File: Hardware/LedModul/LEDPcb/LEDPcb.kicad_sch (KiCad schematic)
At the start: 27 parts, among them J1 Conn_01x01_Pin, J2 Conn_01x01_Pin

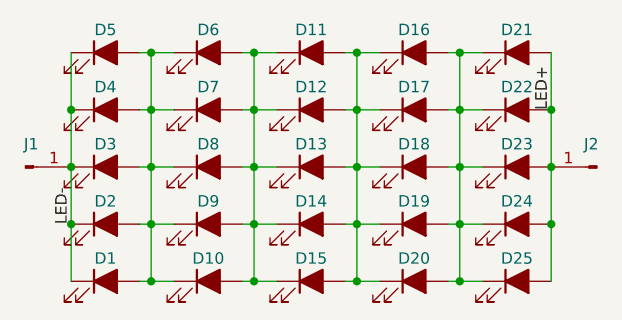
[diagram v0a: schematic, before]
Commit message: added panel
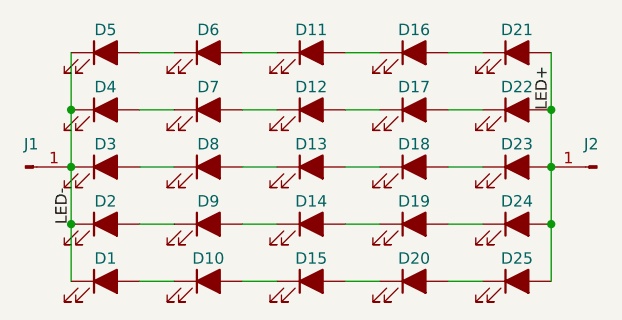
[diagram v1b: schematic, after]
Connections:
- new net: D5.2 (A), D6.1 (K)
- new net: D11.1 (K), D6.2 (A)
- new net: D3.2 (A), D8.1 (K)
- new net: D13.1 (K), D8.2 (A)
- new net: D19.2 (A), D24.1 (K)
- new net: D11.2 (A), D16.1 (K)
- new net: D16.2 (A), D21.1 (K)
- new net: D12.1 (K), D7.2 (A)
- new net: D12.2 (A), D17.1 (K)
- new net: D14.2 (A), D19.1 (K)
- new net: D2.2 (A), D9.1 (K)
- new net: D4.2 (A), D7.1 (K)
- new net: D13.2 (A), D18.1 (K)
- new net: D18.2 (A), D23.1 (K)
- new net: D10.2 (A), D15.1 (K)
- new net: D15.2 (A), D20.1 (K)
- new net: D14.1 (K), D9.2 (A)
- new net: D20.2 (A), D25.1 (K)
- new net: D1.2 (A), D10.1 (K)
- new net: D17.2 (A), D22.1 (K)
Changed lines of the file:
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@@
 (kicad_sch (version 20230121) (generator eeschema)
   (paper "A4")
-  (junction (at 163.83 83.82) (diameter 0) (color 0 0 0 0)
-  )
   (junction (at 196.85 71.12) (diameter 0) (color 0 0 0 0)
-  )
-  (junction (at 163.83 77.47) (diameter 0) (color 0 0 0 0)
-  )
-  (junction (at 175.26 71.12) (diameter 0) (color 0 0 0 0)
   )
   (junction (at 143.51 71.12) (diameter 0) (color 0 0 0 0)
   )
-  (junction (at 186.69 77.47) (diameter 0) (color 0 0 0 0)
-  )
-  (junction (at 152.4 64.77) (diameter 0) (color 0 0 0 0)
-  )
   (junction (at 143.51 77.47) (diameter 0) (color 0 0 0 0)
-  )
-  (junction (at 186.69 83.82) (diameter 0) (color 0 0 0 0)
-  )
-  (junction (at 163.83 71.12) (diameter 0) (color 0 0 0 0)
-  )
-  (junction (at 186.69 64.77) (diameter 0) (color 0 0 0 0)
-  )
-  (junction (at 163.83 64.77) (diameter 0) (color 0 0 0 0)
-  )
-  (junction (at 175.26 83.82) (diameter 0) (color 0 0 0 0)
-  )
-  (junction (at 186.69 71.12) (diameter 0) (color 0 0 0 0)
-  )
-  (junction (at 163.83 90.17) (diameter 0) (color 0 0 0 0)
-  )
-  (junction (at 186.69 90.17) (diameter 0) (color 0 0 0 0)
-  )
-  (junction (at 152.4 83.82) (diameter 0) (color 0 0 0 0)
-  )
-  (junction (at 175.26 77.47) (diameter 0) (color 0 0 0 0)
   )
   (junction (at 143.51 83.82) (diameter 0) (color 0 0 0 0)
   )
-  (junction (at 152.4 71.12) (diameter 0) (color 0 0 0 0)
-  )
   (junction (at 196.85 77.47) (diameter 0) (color 0 0 0 0)
-  )
-  (junction (at 152.4 77.47) (diameter 0) (color 0 0 0 0)
-  )
-  (junction (at 152.4 90.17) (diameter 0) (color 0 0 0 0)
-  )
-  (junction (at 175.26 90.17) (diameter 0) (color 0 0 0 0)
-  )
-  (junction (at 175.26 64.77) (diameter 0) (color 0 0 0 0)
   )
   (junction (at 196.85 83.82) (diameter 0) (color 0 0 0 0)
   )
-  (wire (pts (xy 152.4 77.47) (xy 152.4 83.82))
+  (wire (pts (xy 162.56 71.12) (xy 166.37 71.12))
     (stroke (width 0) (type default))
   )
-  (wire (pts (xy 163.83 71.12) (xy 166.37 71.12))
+  (wire (pts (xy 185.42 71.12) (xy 189.23 71.12))
     (stroke (width 0) (type default))
   )
-  (wire (pts (xy 163.83 83.82) (xy 166.37 83.82))
+  (wire (pts (xy 151.13 83.82) (xy 154.94 83.82))
     (stroke (width 0) (type default))
   )
-  (wire (pts (xy 186.69 71.12) (xy 189.23 71.12))
+  (wire (pts (xy 185.42 83.82) (xy 189.23 83.82))
     (stroke (width 0) (type default))
   )
-  (wire (pts (xy 185.42 83.82) (xy 186.69 83.82))
+  (wire (pts (xy 151.13 64.77) (xy 154.94 64.77))
     (stroke (width 0) (type default))
   )
-  (wire (pts (xy 151.13 83.82) (xy 152.4 83.82))
+  (wire (pts (xy 151.13 90.17) (xy 154.94 90.17))
     (stroke (width 0) (type default))
   )
-  (wire (pts (xy 186.69 83.82) (xy 189.23 83.82))
-    (stroke (width 0) (type default))
-  )
-  (wire (pts (xy 151.13 64.77) (xy 152.4 64.77))
-    (stroke (width 0) (type default))
-  )
-  (wire (pts (xy 152.4 90.17) (xy 154.94 90.17))
-    (stroke (width 0) (type default))
-  )
-  (wire (pts (xy 152.4 71.12) (xy 152.4 77.47))
-    (stroke (width 0) (type default))
-  )
-  (wire (pts (xy 186.69 90.17) (xy 189.23 90.17))
-    (stroke (width 0) (type default))
-  )
-  (wire (pts (xy 173.99 77.47) (xy 175.26 77.47))
-    (stroke (width 0) (type default))
-  )
-  (wire (pts (xy 162.56 77.47) (xy 163.83 77.47))
-    (stroke (width 0) (type default))
-  )
-  (wire (pts (xy 162.56 71.12) (xy 163.83 71.12))
-    (stroke (width 0) (type default))
-  )
-  (wire (pts (xy 186.69 64.77) (xy 186.69 71.12))
+  (wire (pts (xy 173.99 77.47) (xy 177.8 77.47))
     (stroke (width 0) (type default))
   )
@@
     (stroke (width 0) (type default))
   )
-  (wire (pts (xy 163.83 71.12) (xy 163.83 77.47))
-    (stroke (width 0) (type default))
-  )
-  (wire (pts (xy 175.26 90.17) (xy 177.8 90.17))
-    (stroke (width 0) (type default))
-  )
-  (wire (pts (xy 152.4 64.77) (xy 152.4 71.12))
-    (stroke (width 0) (type default))
-  )
-  (wire (pts (xy 152.4 77.47) (xy 154.94 77.47))
-    (stroke (width 0) (type default))
-  )
-  (wire (pts (xy 186.69 77.47) (xy 189.23 77.47))
-    (stroke (width 0) (type default))
-  )
-  (wire (pts (xy 151.13 77.47) (xy 152.4 77.47))
+  (wire (pts (xy 151.13 77.47) (xy 154.94 77.47))
     (stroke (width 0) (type default))
   )
@@
     (stroke (width 0) (type default))
   )
-  (wire (pts (xy 185.42 71.12) (xy 186.69 71.12))
-    (stroke (width 0) (type default))
-  )
-  (wire (pts (xy 152.4 83.82) (xy 152.4 90.17))
-    (stroke (width 0) (type default))
-  )
-  (wire (pts (xy 173.99 64.77) (xy 175.26 64.77))
-    (stroke (width 0) (type default))
-  )
-  (wire (pts (xy 163.83 64.77) (xy 166.37 64.77))
-    (stroke (width 0) (type default))
-  )
-  (wire (pts (xy 151.13 71.12) (xy 152.4 71.12))
+  (wire (pts (xy 173.99 64.77) (xy 177.8 64.77))
     (stroke (width 0) (type default))
   )
@@
     (stroke (width 0) (type default))
   )
-  (wire (pts (xy 152.4 83.82) (xy 154.94 83.82))
-    (stroke (width 0) (type default))
-  )
-  (wire (pts (xy 175.26 64.77) (xy 177.8 64.77))
-    (stroke (width 0) (type default))
-  )
-  (wire (pts (xy 163.83 77.47) (xy 163.83 83.82))
-    (stroke (width 0) (type default))
-  )
   (wire (pts (xy 196.85 71.12) (xy 196.85 77.47))
     (stroke (width 0) (type default))
   )
-  (wire (pts (xy 175.26 71.12) (xy 175.26 77.47))
-    (stroke (width 0) (type default))
-  )
-  (wire (pts (xy 173.99 71.12) (xy 175.26 71.12))
+  (wire (pts (xy 173.99 71.12) (xy 177.8 71.12))
     (stroke (width 0) (type default))
   )
@@
     (stroke (width 0) (type default))
   )
-  (wire (pts (xy 162.56 64.77) (xy 163.83 64.77))
+  (wire (pts (xy 162.56 64.77) (xy 166.37 64.77))
     (stroke (width 0) (type default))
   )
-  (wire (pts (xy 173.99 90.17) (xy 175.26 90.17))
+  (wire (pts (xy 173.99 90.17) (xy 177.8 90.17))
     (stroke (width 0) (type default))
   )
-  (wire (pts (xy 162.56 83.82) (xy 163.83 83.82))
+  (wire (pts (xy 162.56 83.82) (xy 166.37 83.82))
     (stroke (width 0) (type default))
   )
-  (wire (pts (xy 186.69 64.77) (xy 189.23 64.77))
+  (wire (pts (xy 185.42 64.77) (xy 189.23 64.77))
     (stroke (width 0) (type default))
   )
-  (wire (pts (xy 163.83 90.17) (xy 166.37 90.17))
-    (stroke (width 0) (type default))
-  )
-  (wire (pts (xy 186.69 71.12) (xy 186.69 77.47))
-    (stroke (width 0) (type default))
-  )
-  (wire (pts (xy 151.13 90.17) (xy 152.4 90.17))
-    (stroke (width 0) (type default))
-  )
-  (wire (pts (xy 152.4 71.12) (xy 154.94 71.12))
-    (stroke (width 0) (type default))
-  )
-  (wire (pts (xy 173.99 83.82) (xy 175.26 83.82))
+  (wire (pts (xy 151.13 71.12) (xy 154.94 71.12))
     (stroke (width 0) (type default))
   )
@@
     (stroke (width 0) (type default))
   )
-  (wire (pts (xy 175.26 83.82) (xy 175.26 90.17))
+  (wire (pts (xy 162.56 90.17) (xy 166.37 90.17))
     (stroke (width 0) (type default))
   )
-  (wire (pts (xy 162.56 90.17) (xy 163.83 90.17))
-    (stroke (width 0) (type default))
-  )
-  (wire (pts (xy 185.42 64.77) (xy 186.69 64.77))
-    (stroke (width 0) (type default))
-  )
-  (wire (pts (xy 152.4 64.77) (xy 154.94 64.77))
-    (stroke (width 0) (type default))
-  )
-  (wire (pts (xy 175.26 83.82) (xy 177.8 83.82))
+  (wire (pts (xy 173.99 83.82) (xy 177.8 83.82))
     (stroke (width 0) (type default))
   )
@@
     (stroke (width 0) (type default))
   )
-  (wire (pts (xy 175.26 64.77) (xy 175.26 71.12))
+  (wire (pts (xy 162.56 77.47) (xy 166.37 77.47))
     (stroke (width 0) (type default))
   )
-  (wire (pts (xy 163.83 77.47) (xy 166.37 77.47))
+  (wire (pts (xy 185.42 90.17) (xy 189.23 90.17))
     (stroke (width 0) (type default))
   )
-  (wire (pts (xy 175.26 71.12) (xy 177.8 71.12))
-    (stroke (width 0) (type default))
-  )
-  (wire (pts (xy 175.26 77.47) (xy 175.26 83.82))
-    (stroke (width 0) (type default))
-  )
-  (wire (pts (xy 163.83 64.77) (xy 163.83 71.12))
-    (stroke (width 0) (type default))
-  )
-  (wire (pts (xy 185.42 90.17) (xy 186.69 90.17))
-    (stroke (width 0) (type default))
-  )
-  (wire (pts (xy 185.42 77.47) (xy 186.69 77.47))
+  (wire (pts (xy 185.42 77.47) (xy 189.23 77.47))
     (stroke (width 0) (type default))
   )
@@
     (stroke (width 0) (type default))
   )
-  (wire (pts (xy 163.83 83.82) (xy 163.83 90.17))
-    (stroke (width 0) (type default))
-  )
-  (wire (pts (xy 175.26 77.47) (xy 177.8 77.47))
-    (stroke (width 0) (type default))
-  )
-  (wire (pts (xy 186.69 83.82) (xy 186.69 90.17))
-    (stroke (width 0) (type default))
-  )
-  (wire (pts (xy 186.69 77.47) (xy 186.69 83.82))
-    (stroke (width 0) (type default))
-  )

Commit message: V1.1
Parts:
- added J3, J4: Conn_01x01_Pin, Bergi:S9141-45R, symbol Connector:Conn_01x01_Pin
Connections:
- net LED+: now also J4.1 (Pin_1)
- net LED-: now also J3.1 (Pin_1)
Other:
- moved on the sheet: J1, J2
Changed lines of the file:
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@@
+    (stroke (width 0) (type default))
+  )
+  (wire (pts (xy 143.51 64.77) (xy 143.51 71.12))
     (stroke (width 0) (type default))
   )
@@
     (stroke (width 0) (type default))
   )
-  (wire (pts (xy 143.51 64.77) (xy 143.51 71.12))
-    (stroke (width 0) (type default))
-  )
   (wire (pts (xy 173.99 64.77) (xy 177.8 64.77))
     (stroke (width 0) (type default))
   )
+  (wire (pts (xy 196.85 71.12) (xy 196.85 77.47))
+    (stroke (width 0) (type default))
+  )
+  (wire (pts (xy 173.99 71.12) (xy 177.8 71.12))
+    (stroke (width 0) (type default))
+  )
+  (wire (pts (xy 143.51 77.47) (xy 143.51 83.82))
+    (stroke (width 0) (type default))
+  )
+  (wire (pts (xy 162.56 64.77) (xy 166.37 64.77))
+    (stroke (width 0) (type default))
+  )
+  (wire (pts (xy 173.99 90.17) (xy 177.8 90.17))
+    (stroke (width 0) (type default))
+  )
+  (wire (pts (xy 162.56 83.82) (xy 166.37 83.82))
+    (stroke (width 0) (type default))
+  )
+  (wire (pts (xy 185.42 64.77) (xy 189.23 64.77))
+    (stroke (width 0) (type default))
+  )
+  (wire (pts (xy 151.13 71.12) (xy 154.94 71.12))
+    (stroke (width 0) (type default))
+  )
+  (wire (pts (xy 196.85 77.47) (xy 196.85 83.82))
+    (stroke (width 0) (type default))
+  )
+  (wire (pts (xy 162.56 90.17) (xy 166.37 90.17))
+    (stroke (width 0) (type default))
+  )
   (wire (pts (xy 196.85 64.77) (xy 196.85 71.12))
-    (stroke (width 0) (type default))
-  )
-  (wire (pts (xy 196.85 71.12) (xy 196.85 77.47))
-    (stroke (width 0) (type default))
-  )
-  (wire (pts (xy 173.99 71.12) (xy 177.8 71.12))
-    (stroke (width 0) (type default))
-  )
-  (wire (pts (xy 143.51 77.47) (xy 143.51 83.82))
-    (stroke (width 0) (type default))
-  )
-  (wire (pts (xy 162.56 64.77) (xy 166.37 64.77))
-    (stroke (width 0) (type default))
-  )
-  (wire (pts (xy 173.99 90.17) (xy 177.8 90.17))
-    (stroke (width 0) (type default))
-  )
-  (wire (pts (xy 162.56 83.82) (xy 166.37 83.82))
-    (stroke (width 0) (type default))
-  )
-  (wire (pts (xy 185.42 64.77) (xy 189.23 64.77))
-    (stroke (width 0) (type default))
-  )
-  (wire (pts (xy 151.13 71.12) (xy 154.94 71.12))
-    (stroke (width 0) (type default))
-  )
-  (wire (pts (xy 196.85 77.47) (xy 196.85 83.82))
-    (stroke (width 0) (type default))
-  )
-  (wire (pts (xy 162.56 90.17) (xy 166.37 90.17))
     (stroke (width 0) (type default))
   )
@@
     )
   )
+  (symbol (lib_id "Connector:Conn_01x01_Pin") (at 138.43 71.12 0) (unit 1)
+    (in_bom yes) (on_board yes) (dnp no) (fields_autoplaced)
+    (property "Reference" "J3" (at 139.065 68.58 0)
+      (effects (font (size 1.27 1.27)))
+    )
+    (property "Value" "Conn_01x01_Pin" (at 139.065 68.58 0)
+      (effects (font (size 1.27 1.27)) hide)
+    )
+    (property "Footprint" "Bergi:S9141-45R" (at 138.43 71.12 0)
+      (effects (font (size 1.27 1.27)) hide)
+    )
+    (property "Datasheet" "~" (at 138.43 71.12 0)
+      (effects (font (size 1.27 1.27)) hide)
+    )
+    (pin "1")
+    (instances
+      (project "LEDPcb"
+        (path "/a80acc9f-be1a-4cc9-b2de-6c618576ddc1"
+          (reference "J3") (unit 1)
+        )
+      )
+    )
+  )
   (symbol (lib_id "Device:LED_Filled") (at 158.75 77.47 0) (unit 1)
     (in_bom yes) (on_board yes) (dnp no)
@@
     )
   )
-  (symbol (lib_id "Connector:Conn_01x01_Pin") (at 138.43 77.47 0) (unit 1)
+  (symbol (lib_id "Connector:Conn_01x01_Pin") (at 138.43 83.82 0) (unit 1)
     (in_bom yes) (on_board yes) (dnp no) (fields_autoplaced)
-    (property "Reference" "J1" (at 139.065 74.93 0)
-      (effects (font (size 1.27 1.27)))
-    )
-    (property "Value" "Conn_01x01_Pin" (at 139.065 74.93 0)
-      (effects (font (size 1.27 1.27)) hide)
-    )
-    (property "Footprint" "Bergi:Solderpad_1x2" (at 138.43 77.47 0)
-      (effects (font (size 1.27 1.27)) hide)
-    )
-    (property "Datasheet" "~" (at 138.43 77.47 0)
+    (property "Reference" "J1" (at 139.065 81.28 0)
+      (effects (font (size 1.27 1.27)))
+    )
+    (property "Value" "Conn_01x01_Pin" (at 139.065 81.28 0)
+      (effects (font (size 1.27 1.27)) hide)
+    )
+    (property "Footprint" "Bergi:Solderpad_1x2" (at 138.43 83.82 0)
+      (effects (font (size 1.27 1.27)) hide)
+    )
+    (property "Datasheet" "~" (at 138.43 83.82 0)
       (effects (font (size 1.27 1.27)) hide)
     )
@@
     )
   )
+  (symbol (lib_id "Connector:Conn_01x01_Pin") (at 201.93 71.12 180) (unit 1)
+    (in_bom yes) (on_board yes) (dnp no) (fields_autoplaced)
+    (property "Reference" "J4" (at 201.295 68.58 0)
+      (effects (font (size 1.27 1.27)))
+    )
+    (property "Value" "Conn_01x01_Pin" (at 201.295 73.66 0)
+      (effects (font (size 1.27 1.27)) hide)
+    )
+    (property "Footprint" "Bergi:S9141-45R" (at 201.93 71.12 0)
+      (effects (font (size 1.27 1.27)) hide)
+    )
+    (property "Datasheet" "~" (at 201.93 71.12 0)
+      (effects (font (size 1.27 1.27)) hide)
+    )
+    (pin "1")
+    (instances
+      (project "LEDPcb"
+        (path "/a80acc9f-be1a-4cc9-b2de-6c618576ddc1"
+          (reference "J4") (unit 1)
+        )
+      )
+    )
+  )
   (symbol (lib_id "Device:LED_Filled") (at 170.18 83.82 0) (unit 1)
     (in_bom yes) (on_board yes) (dnp no)
@@
     )
   )
-  (symbol (lib_id "Connector:Conn_01x01_Pin") (at 201.93 77.47 180) (unit 1)
+  (symbol (lib_id "Connector:Conn_01x01_Pin") (at 201.93 83.82 180) (unit 1)
     (in_bom yes) (on_board yes) (dnp no) (fields_autoplaced)
-    (property "Reference" "J2" (at 201.295 74.93 0)
-      (effects (font (size 1.27 1.27)))
-    )
-    (property "Value" "Conn_01x01_Pin" (at 201.295 80.01 0)
-      (effects (font (size 1.27 1.27)) hide)
-    )
-    (property "Footprint" "Bergi:Solderpad_1x2" (at 201.93 77.47 0)
-      (effects (font (size 1.27 1.27)) hide)
-    )
-    (property "Datasheet" "~" (at 201.93 77.47 0)
-      (effects (font (size 1.27 1.27)) hide)
-    )
+    (property "Reference" "J2" (at 201.295 81.28 0)
+      (effects (font (size 1.27 1.27)))
+    )
+    (property "Value" "Conn_01x01_Pin" (at 201.295 86.36 0)
+      (effects (font (size 1.27 1.27)) hide)
+    )
+    (property "Footprint" "Bergi:Solderpad_1x2" (at 201.93 83.82 0)
+      (effects (font (size 1.27 1.27)) hide)
+    )
+    (property "Datasheet" "~" (at 201.93 83.82 0)
+      (effects (font (size 1.27 1.27)) hide)
+    )
